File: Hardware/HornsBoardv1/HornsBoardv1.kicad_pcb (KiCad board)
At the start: 2 copper layers, 53 x 34 mm, 21 parts, among them J2 Conn_01x02, J3 Conn_01x02, J4 Conn_01x02

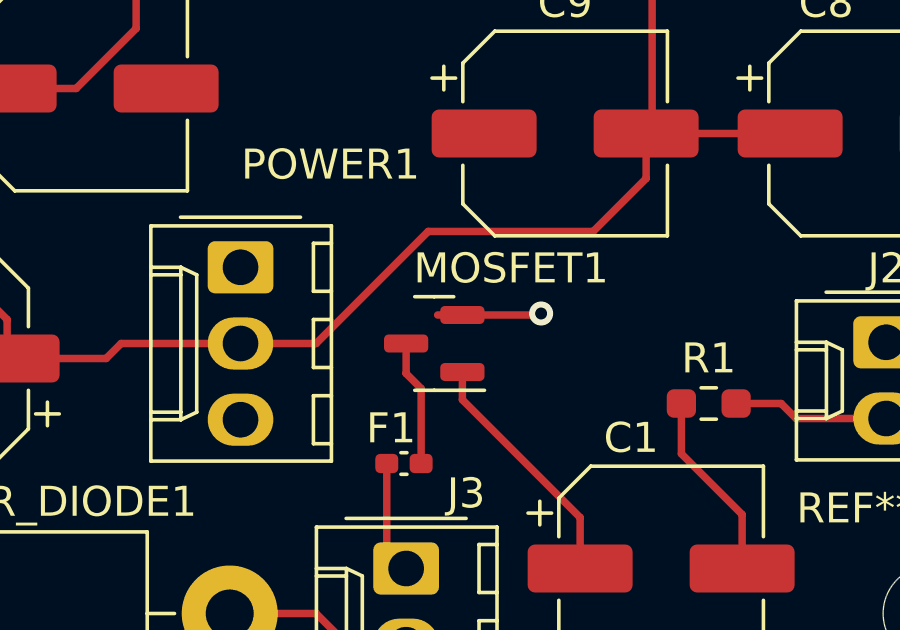
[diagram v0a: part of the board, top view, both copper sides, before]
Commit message: Traces fixed for both hardware
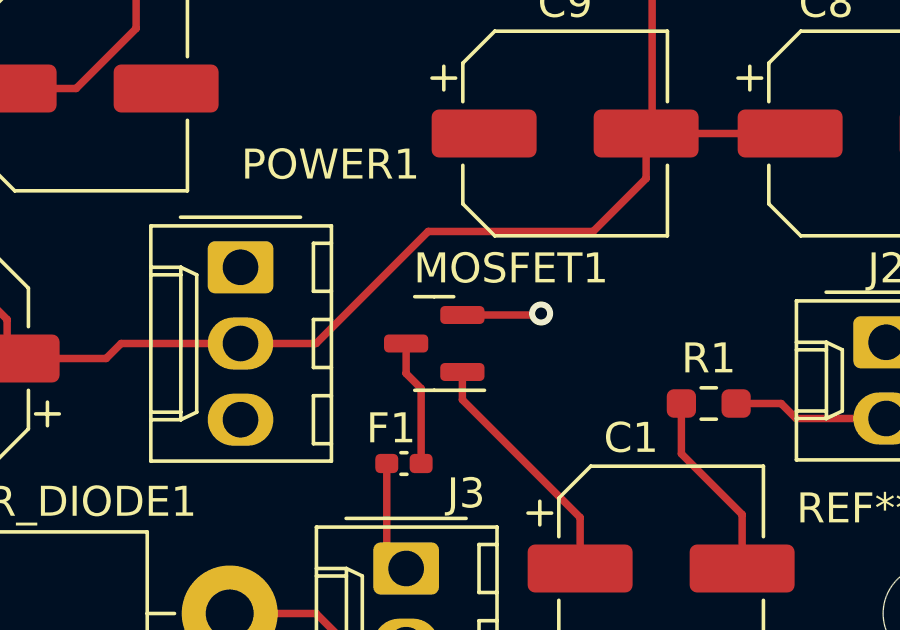
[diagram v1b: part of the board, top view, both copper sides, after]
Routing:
- net GND: track 3.47 -> 2.65 mm
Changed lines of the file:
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@@
-		(net 5)
-	)
-	(segment
-		(start 105.375 93.05)
-		(end 104.55 93.05)
-		(width 0.25)
-		(layer "F.Cu")
 		(net 5)
 	)
